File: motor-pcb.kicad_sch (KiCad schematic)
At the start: 20 parts, among them J1 Power Input, J2 Motor, J3 Optocoupler, J5 Connection with second PCB, U1 LM7812_TO220, U2 INA219BxDCN, U3 LM7805_TO220, U4 TMP117xxDRV

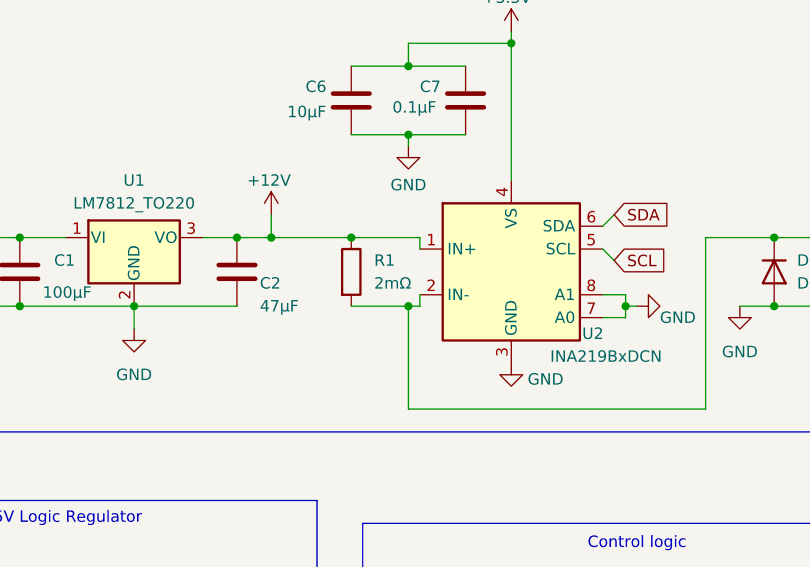
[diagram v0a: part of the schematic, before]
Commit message: Updated shunt resistor value, footprints, layout
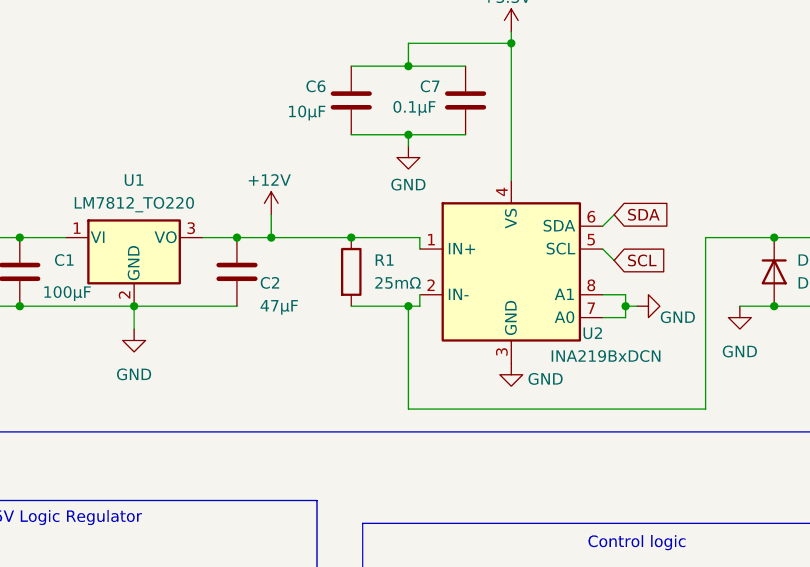
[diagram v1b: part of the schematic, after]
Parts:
- C1, C4: footprint Capacitor_THT:CP_Radial_D6.3mm_P2.50mm -> Capacitor_THT:CP_Radial_D8.0mm_P3.50mm
- C6: footprint Capacitor_SMD:C_0805_2012Metric_Pad1.18x1.45mm_HandSolder -> Capacitor_THT:CP_Radial_D5.0mm_P2.00mm
- C7: footprint Capacitor_SMD:C_0805_2012Metric_Pad1.18x1.45mm_HandSolder -> Capacitor_THT:C_Disc_D5.0mm_W2.5mm_P2.50mm
- R1: value 2mΩ -> 25mΩ; footprint Resistor_SMD:R_2512_6332Metric_Pad1.40x3.35mm_HandSolder -> Resistor_THT:R_Axial_DIN0414_L11.9mm_D4.5mm_P15.24mm_Horizonta
- R2: footprint Resistor_THT:R_Axial_DIN0207_L6.3mm_D2.5mm_P7.62mm_Horizontal -> Resistor_THT:R_Axial_DIN0207_L6.3mm_D2.5mm_P10.16mm_Horizontal
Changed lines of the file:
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@@
 			)
 		)
-		(property "Footprint" "Capacitor_THT:CP_Radial_D6.3mm_P2.50mm"
+		(property "Footprint" "Capacitor_THT:CP_Radial_D8.0mm_P3.50mm"
 			(at 61.9252 120.65 0)
 			(hide yes)
@@
 			)
 		)
-		(property "Footprint" "Resistor_THT:R_Axial_DIN0207_L6.3mm_D2.5mm_P7.62mm_Horizontal"
+		(property "Footprint" "Resistor_THT:R_Axial_DIN0207_L6.3mm_D2.5mm_P10.16mm_Horizontal"
 			(at 142.24 113.538 90)
 			(hide yes)
@@
 			)
 		)
-		(property "Footprint" "Capacitor_SMD:C_0805_2012Metric_Pad1.18x1.45mm_HandSolder"
+		(property "Footprint" "Capacitor_THT:CP_Radial_D5.0mm_P2.00mm"
 			(at 105.1052 55.88 0)
 			(hide yes)
@@
 			)
 		)
-		(property "Footprint" "Capacitor_SMD:C_0805_2012Metric_Pad1.18x1.45mm_HandSolder"
+		(property "Footprint" "Capacitor_THT:C_Disc_D5.0mm_W2.5mm_P2.50mm"
 			(at 117.8052 55.88 0)
 			(hide yes)
@@
 			)
 		)
-		(property "Value" "2mΩ"
+		(property "Value" "25mΩ"
 			(at 106.68 72.3899 0)
 			(show_name no)
@@
 			)
 		)
-		(property "Footprint" "Resistor_SMD:R_2512_6332Metric_Pad1.40x3.35mm_HandSolder"
+		(property "Footprint" "Resistor_THT:R_Axial_DIN0414_L11.9mm_D4.5mm_P15.24mm_Horizonta"
 			(at 102.362 71.12 90)
 			(hide yes)
@@
 			)
 		)
-		(property "Footprint" "Capacitor_THT:CP_Radial_D6.3mm_P2.50mm"
+		(property "Footprint" "Capacitor_THT:CP_Radial_D8.0mm_P3.50mm"
 			(at 68.2752 74.93 0)
 			(hide yes)
